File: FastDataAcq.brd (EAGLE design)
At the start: 114.3 x 63.5 mm, 215 parts, among them J1 MICRO-FIT_3.0_2POS_RA_SMD, J2 USB_MICROAB_SMT, U1 ADC08D500, U10 TMP421, U11 DAC101C081, U12 ADCMP553BRMZ, U13 XCFXXS04, U14 FT230XQ, U2 XC6SLX9-3TQG144C, U3 LTC2955-1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

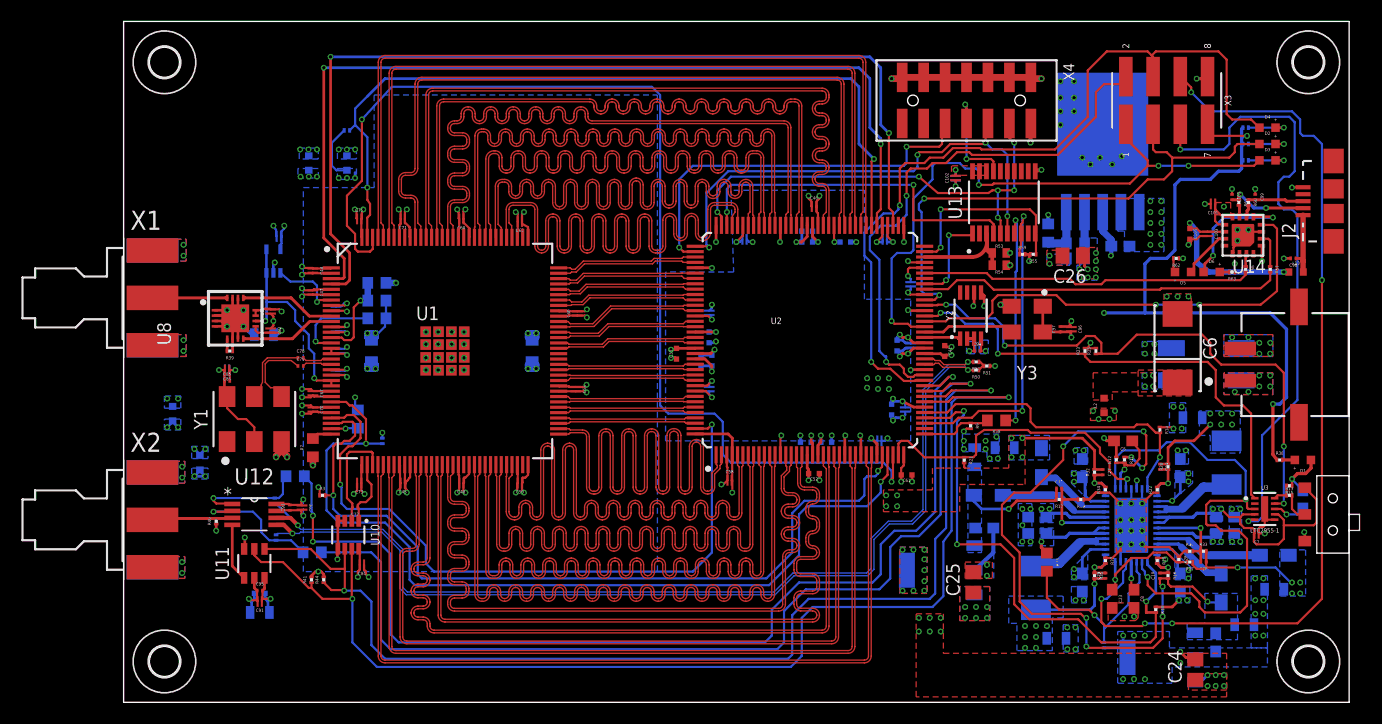
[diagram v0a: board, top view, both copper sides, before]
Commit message: FDA v0.9 Ready For Quote Submission
All that is left is shielding mounting holes.
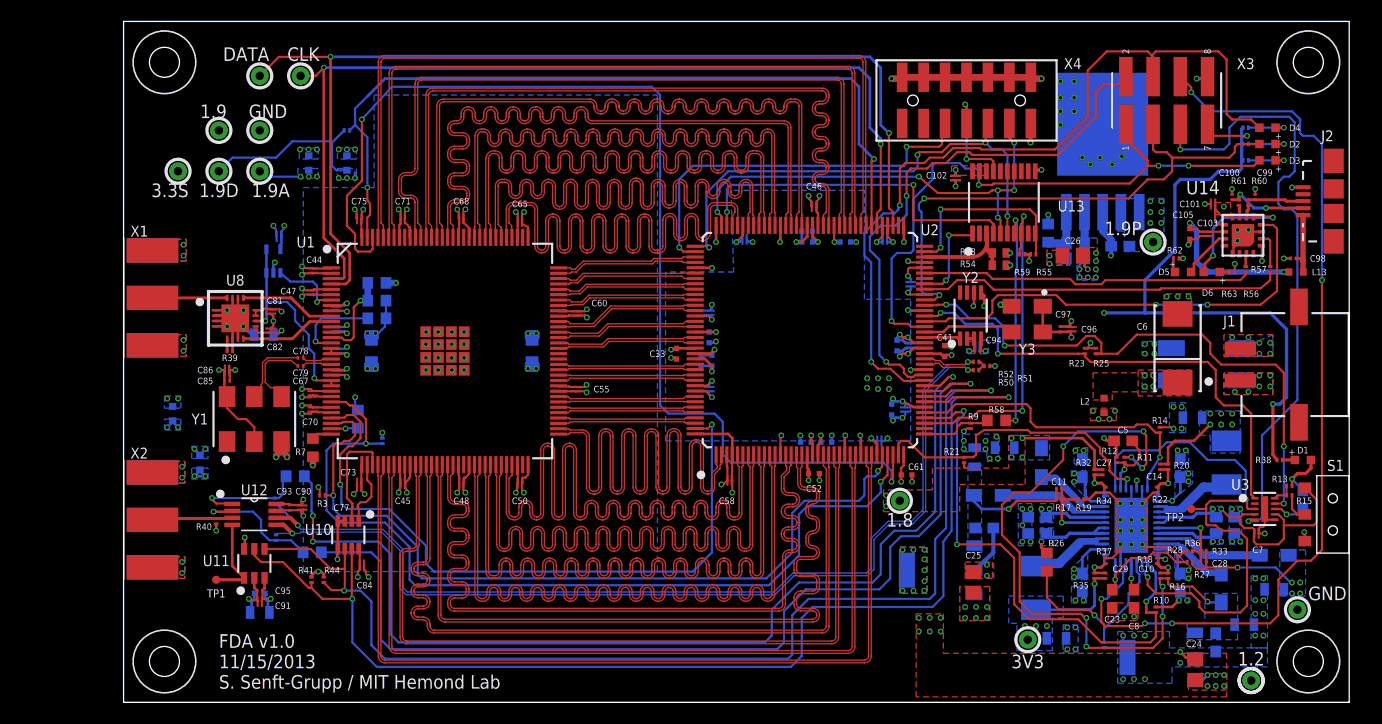
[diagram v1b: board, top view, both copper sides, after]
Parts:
- added TP1, TP2: TEST-POINT3, SparkFun-Passives:PAD.03X.03
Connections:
- net PWR_ENABLE: now also TP2.P$1
- net TRIG_REF: now also TP1.P$1
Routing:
- net 1V9D: track 31.3 -> 43.1 mm, vias 14 -> 15
- net ADC_OUTEDGE/DDR/SDATA: track 90.3 -> 97.7 mm, vias 2 -> 3
- net 1V9A: track 33.4 -> 37.4 mm, vias 18 -> 19
- net TRIG_REF: track 5.41 -> 8.08 mm
- net ADC_OUTV/SCLK: track 87.2 -> 89.7 mm, vias 2 -> 3
- net PWR_ENABLE: track 50.6 -> 52.0 mm
- net 3V3: track 125.7 -> 124.8 mm, vias 34 -> 31
- net S_TEMP: track 87.9 -> 87.1 mm
- net GND: vias 214 -> 216
- net 3V3S: vias 5 -> 6
- net 2V3_1V9PRE: vias 16 -> 13
- net 1V9: vias 14 -> 15
- net 1V8: vias 17 -> 16
- net 1V2: vias 16 -> 17
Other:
- board text added: "1.2"
- board text added: "1.8"
- board text added: "1.9"
- board text added: "1.9A"
- board text added: "1.9D"
- board text added: "1.9P"
- board text added: "11/15/2013"
- board text added: "3.3S"
- board text added: "3V3"
- board text added: "CLK"
- board text added: "DATA"
- board text added: "FDA v1.0"
- board text added: "GND"
- board text added: "S. Senft-Grupp / MIT Hemond Lab"
- board text added: "TP1"
- board text added: "TP2"

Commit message: Neatened back traces.
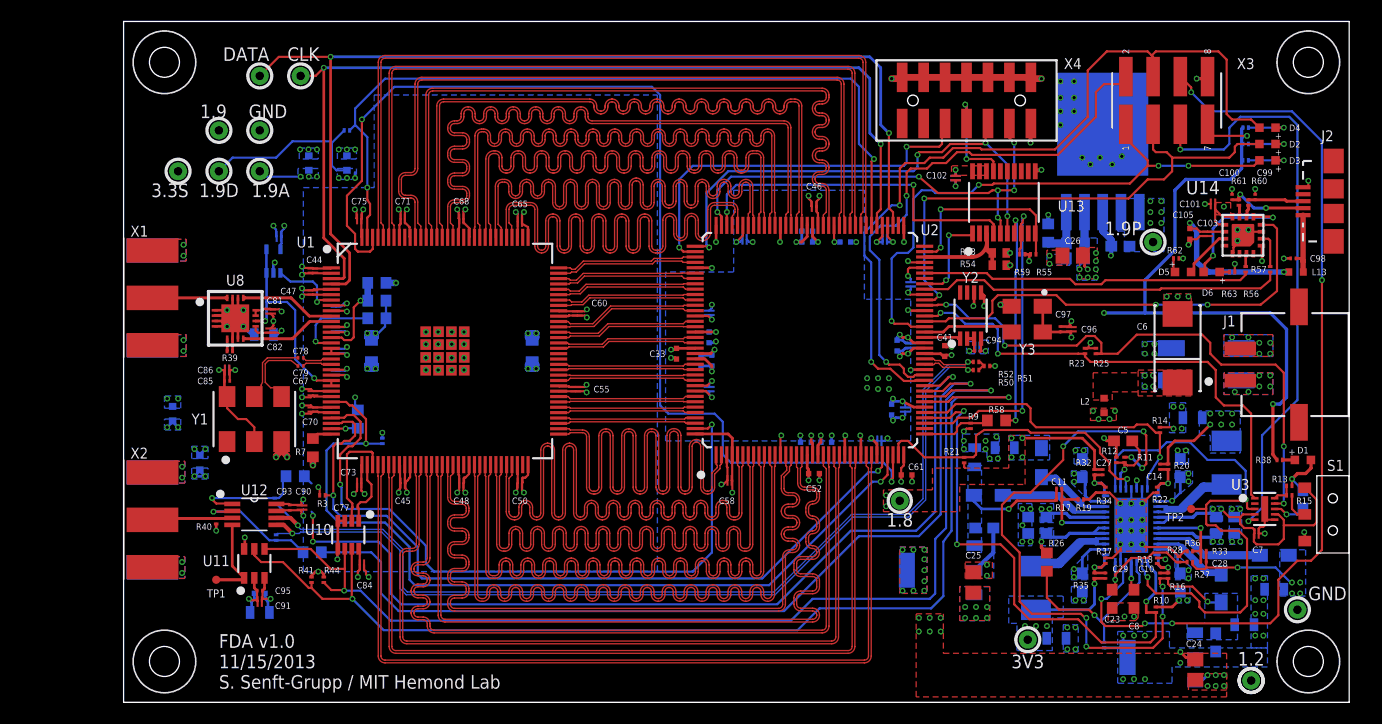
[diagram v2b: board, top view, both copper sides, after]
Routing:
- net TRIG_RESET_LOW: track 97.4 -> 86.6 mm
- net TRIG_RESET_HIGH: track 93.3 -> 84.3 mm
- net FPGA_SDA: track 108.7 -> 101.2 mm
- net FPGA_SCL: track 113.4 -> 106.1 mm
- net ADC_CAL: track 76.4 -> 73.2 mm
- net FPGA_GPIO3: track 58.0 -> 54.9 mm
- net ADC_PD: track 83.2 -> 80.4 mm
- net !PB: track 57.8 -> 55.3 mm
- net FPGA_TRIG_N: track 92.9 -> 90.7 mm
- net FPGA_TRIG_P: track 94.5 -> 92.2 mm
- net FPGA_GPIO4: track 51.4 -> 50.0 mm
- net N$20: track 12.5 -> 11.9 mm
- net S_TEMP: track 87.1 -> 86.5 mm
- net S_MODE: track 18.2 -> 17.6 mm
- net FPGA_TCK: track 47.4 -> 46.9 mm

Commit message: Minor Changes - Fixed Screw Holes
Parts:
- added PAD1, PAD2, PAD3, PAD4: (no value), wirepad:SMD1,27-2,54
- H1, H2, H3, H4: value MOUNT-HOLE2.8 -> MOUNT-HOLE2.0; device holes:2,8 -> holes:2.0
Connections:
- net GND: now also PAD1.1, PAD2.1, PAD3.1, PAD4.1
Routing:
- net GND: track 233.8 -> 243.5 mm, vias 216 -> 219
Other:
- board text added: "OFF"
- board text added: "ON"
- board text removed: "Manufacturer Notes: 1. All copper thickness is 1oz 2. LVDS lines are 5mil width with 5mil spacing and should have a 100 Ohms+/- 10% differential impedance."
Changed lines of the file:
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@@
 <layer number="1" name="Top" color="4" fill="1" visible="yes" active="yes"/>
 <layer number="2" name="GND" color="1" fill="3" visible="no" active="yes"/>
-<layer number="3" name="Power" color="3" fill="3" visible="no" active="yes"/>
+<layer number="3" name="Power" color="3" fill="3" visible="yes" active="yes"/>
 <layer number="14" name="Route14" color="1" fill="6" visible="no" active="no"/>
 <layer number="15" name="Route15" color="4" fill="6" visible="no" active="no"/>
@@
 <layer number="17" name="Pads" color="2" fill="1" visible="yes" active="yes"/>
 <layer number="18" name="Vias" color="2" fill="1" visible="yes" active="yes"/>
-<layer number="19" name="Unrouted" color="6" fill="1" visible="no" active="yes"/>
+<layer number="19" name="Unrouted" color="6" fill="1" visible="yes" active="yes"/>
 <layer number="20" name="Dimension" color="15" fill="1" visible="yes" active="yes"/>
 <layer number="21" name="tPlace" color="7" fill="1" visible="yes" active="yes"/>
-<layer number="22" name="bPlace" color="7" fill="1" visible="yes" active="yes"/>
+<layer number="22" name="bPlace" color="7" fill="1" visible="no" active="yes"/>
 <layer number="23" name="tOrigins" color="15" fill="1" visible="yes" active="yes"/>
-<layer number="24" name="bOrigins" color="15" fill="1" visible="yes" active="yes"/>
+<layer number="24" name="bOrigins" color="15" fill="1" visible="no" active="yes"/>
 <layer number="25" name="tNames" color="7" fill="1" visible="yes" active="yes"/>
-<layer number="26" name="bNames" color="7" fill="1" visible="yes" active="yes"/>
+<layer number="26" name="bNames" color="7" fill="1" visible="no" active="yes"/>
 <layer number="27" name="tValues" color="7" fill="1" visible="no" active="yes"/>
 <layer number="28" name="bValues" color="7" fill="1" visible="no" active="yes"/>
@@
 <layer number="49" name="Reference" color="7" fill="1" visible="no" active="yes"/>
 <layer number="50" name="dxf" color="7" fill="1" visible="no" active="no"/>
-<layer number="51" name="tDocu" color="14" fill="1" visible="no" active="yes"/>
+<layer number="51" name="tDocu" color="14" fill="1" visible="yes" active="yes"/>
 <layer number="52" name="bDocu" color="14" fill="1" visible="no" active="yes"/>
 <layer number="53" name="tGND_GNDA" color="7" fill="9" visible="no" active="no"/>
@@
 <wire x1="114.3" y1="63.5" x2="0" y2="63.5" width="0" layer="20"/>
 <wire x1="0" y1="63.5" x2="0" y2="0" width="0" layer="20"/>
-<text x="0.127" y="68.834" size="0.6096" layer="51">Manufacturer Notes:
-1. All copper thickness is 1oz
-2. LVDS lines are 5mil width with 5mil spacing and should have a  100 Ohms+/- 10% differential impedance.</text>
 <text x="13.462" y="55.118" size="1.27" layer="21" font="vector" align="center">GND</text>
 <text x="8.382" y="55.118" size="1.27" layer="21" font="vector" align="center">1.9</text>
@@
 <text x="84.328" y="3.81" size="1.27" layer="21" font="vector" align="center">3V3</text>
 <text x="72.39" y="17.018" size="1.27" layer="21" font="vector" align="center">1.8</text>
-<text x="112.268" y="10.16" size="1.27" layer="21" font="vector" align="center">GND</text>
+<text x="108.966" y="6.604" size="1.27" layer="21" font="vector" align="center">GND</text>
 <text x="93.218" y="44.196" size="1.27" layer="21" font="vector" align="center">1.9P</text>
 <circle x="5.08" y="49.53" radius="1.1176" width="0.3048" layer="21"/>
@@
 <text x="8.89" y="5.08" size="1.27" layer="21" font="vector">FDA v1.0</text>
 <text x="8.89" y="3.175" size="1.27" layer="21" font="vector">11/15/2013</text>
+<text x="113.284" y="21.59" size="1.27" layer="21" font="vector" rot="R90">ON</text>
+<text x="113.284" y="13.843" size="1.27" layer="21" font="vector" rot="R90" align="bottom-right">OFF</text>
+<circle x="3.81" y="59.69" radius="2" width="0.4064" layer="21"/>
 </plain>
 <attributes>
@@
 <attribute name="VALUE" x="77.7578" y="22.5924" size="0.6096" layer="27" font="vector" rot="R270" align="center"/>
 </element>
-<element name="H1" library="holes" package="2,8" value="MOUNT-HOLE2.8" x="110.49" y="3.81" smashed="yes"/>
-<element name="H2" library="holes" package="2,8" value="MOUNT-HOLE2.8" x="110.49" y="59.69" smashed="yes" rot="R90"/>
-<element name="H3" library="holes" package="2,8" value="MOUNT-HOLE2.8" x="3.81" y="3.81" smashed="yes" rot="R90"/>
-<element name="H4" library="holes" package="2,8" value="MOUNT-HOLE2.8" x="3.81" y="59.69" smashed="yes"/>
+<element name="H1" library="holes" package="2.0" value="MOUNT-HOLE2.0" x="110.49" y="3.81" smashed="yes"/>
+<element name="H2" library="holes" package="2.0" value="MOUNT-HOLE2.0" x="110.49" y="59.69" smashed="yes" rot="R90"/>
+<element name="H3" library="holes" package="2.0" value="MOUNT-HOLE2.0" x="3.81" y="3.81" smashed="yes" rot="R90"/>
+<element name="H4" library="holes" package="2.0" value="MOUNT-HOLE2.0" x="3.81" y="59.69" smashed="yes"/>
 <element name="D1" library="Schuyler" package="0603_LED" value="LED_0603_RED" x="109.982" y="22.606" smashed="yes" rot="R180">
 <attribute name="MANUFACTURER" value="" x="109.982" y="22.606" size="1.778" layer="27" rot="R180" display="off"/>
@@
 <attribute name="PARTNUMBER" value="401-2012-1-ND" x="112.776" y="17.526" size="1.778" layer="27" rot="R90" display="off"/>
 <attribute name="MANPARTNUMBER" value="AYZ0102AGRLC" x="112.776" y="17.526" size="1.778" layer="27" rot="R90" display="off"/>
-<attribute name="NAME" x="113.03" y="22.098" size="1.016" layer="25" font="vector" rot="R180" align="center"/>
+<attribute name="NAME" x="108.966" y="14.224" size="1.016" layer="25" font="vector" rot="R180" align="center"/>
 </element>
 <element name="R14" library="rcl" package="R0201" value="523K" x="96.647" y="25.4" smashed="yes" rot="R270">
@@
 <attribute name="PARTNUMBER" value="WM17450-ND" x="97.282" y="56.134" size="1.778" layer="27" display="off"/>
 <attribute name="MANPARTNUMBER" value="0015912080" x="97.282" y="56.134" size="1.778" layer="27" display="off"/>
-<attribute name="NAME" x="104.648" y="59.563" size="1.016" layer="21" font="vector" rot="R180" align="center"/>
+<attribute name="NAME" x="104.14" y="56.134" size="1.016" layer="21" font="vector" rot="R180" align="center"/>
 </element>
 <element name="TP1" library="SparkFun-Passives" package="PAD.03X.03" value="TEST-POINT3" x="8.636" y="11.43"/>
 <element name="TP2" library="SparkFun-Passives" package="PAD.03X.03" value="TEST-POINT3" x="99.568" y="18.034"/>
+<element name="PAD2" library="wirepad" package="SMD1,27-2,54" value="" x="112.014" y="8.636"/>
+<element name="PAD1" library="wirepad" package="SMD1,27-2,54" value="" x="3.81" y="8.636" rot="R90"/>
+<element name="PAD3" library="wirepad" package="SMD1,27-2,54" value="" x="3.81" y="54.864"/>
+<element name="PAD4" library="wirepad" package="SMD1,27-2,54" value="" x="105.664" y="60.706"/>
 </elements>
 <signals>
@@
 <wire x1="110.393" y1="48.036" x2="110.49" y2="48.133" width="0.2032" layer="1"/>
 <wire x1="110.49" y1="48.133" x2="110.49" y2="48.641" width="0.2032" layer="1"/>
+<contactref element="PAD4" pad="1"/>
+<contactref element="PAD3" pad="1"/>
+<contactref element="PAD2" pad="1"/>
+<contactref element="PAD1" pad="1"/>
+<via x="6.858" y="8.636" extent="1-16" drill="0.3048"/>
+<wire x1="6.858" y1="8.636" x2="3.81" y2="8.636" width="0.6096" layer="1"/>
+<via x="5.842" y="54.864" extent="1-16" drill="0.3048"/>
+<wire x1="3.81" y1="54.864" x2="5.842" y2="54.864" width="0.6096" layer="1"/>
+<wire x1="109.474" y1="8.636" x2="112.014" y2="8.636" width="0.6096" layer="1"/>
+<via x="105.664" y="58.674" extent="1-16" drill="0.3048"/>
+<wire x1="105.664" y1="58.674" x2="105.664" y2="60.706" width="0.6096" layer="1"/>
 </signal>
 <signal name="N$8">

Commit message: More minor fixes.
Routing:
- net FPGA_TDO: track 32.5 -> 31.6 mm
- net CLK500_N: track 6.99 -> 6.29 mm
- net CLK500_P: track 7.27 -> 6.63 mm

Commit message: Ready for quote submittal.
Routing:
- net GND: track 243.2 -> 241.7 mm

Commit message: Done with adjusting most of the LVDS track widths.
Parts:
- added R64, R65, R66, R67: 330, rcl:R0201
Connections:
- new net N$23: R65.1, X3.P$2
- new net N$25: R66.1, X3.P$3
- new net N$26: R67.1, X3.P$4
- new net N$9: R64.1, X3.P$1
- net FPGA_GPIO1: now also R67.2; no longer X3.P$4
- net FPGA_GPIO2: now also R65.2; no longer X3.P$2
- net FPGA_GPIO3: now also R64.2; no longer X3.P$1
- net FPGA_GPIO4: now also R66.2; no longer X3.P$3
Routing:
- net N$26: track 0.00 -> 12.7 mm
- net ADC_DCLKRST: track 8.22 -> 0.00 mm, vias 1 -> 0
- net FPGA_GPIO2: track 51.5 -> 43.3 mm
- net N$9: track 0.00 -> 7.79 mm
- net N$23: track 0.00 -> 7.74 mm
- net FPGA_GPIO4: track 50.0 -> 44.5 mm
- net N$25: track 0.00 -> 4.00 mm
- net FPGA_TDI: track 37.0 -> 40.8 mm
- net FPGA_GPIO3: track 54.9 -> 51.3 mm
- net DQD0_N: track 82.6 -> 81.2 mm
- net DQD0_P: track 83.1 -> 82.0 mm
- net FPGA_GPIO1: track 74.8 -> 73.7 mm
- net DQD5_P: track 73.2 -> 74.2 mm
- net DQD2_P: track 75.5 -> 76.5 mm
- net DQD2_N: track 74.8 -> 75.8 mm
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
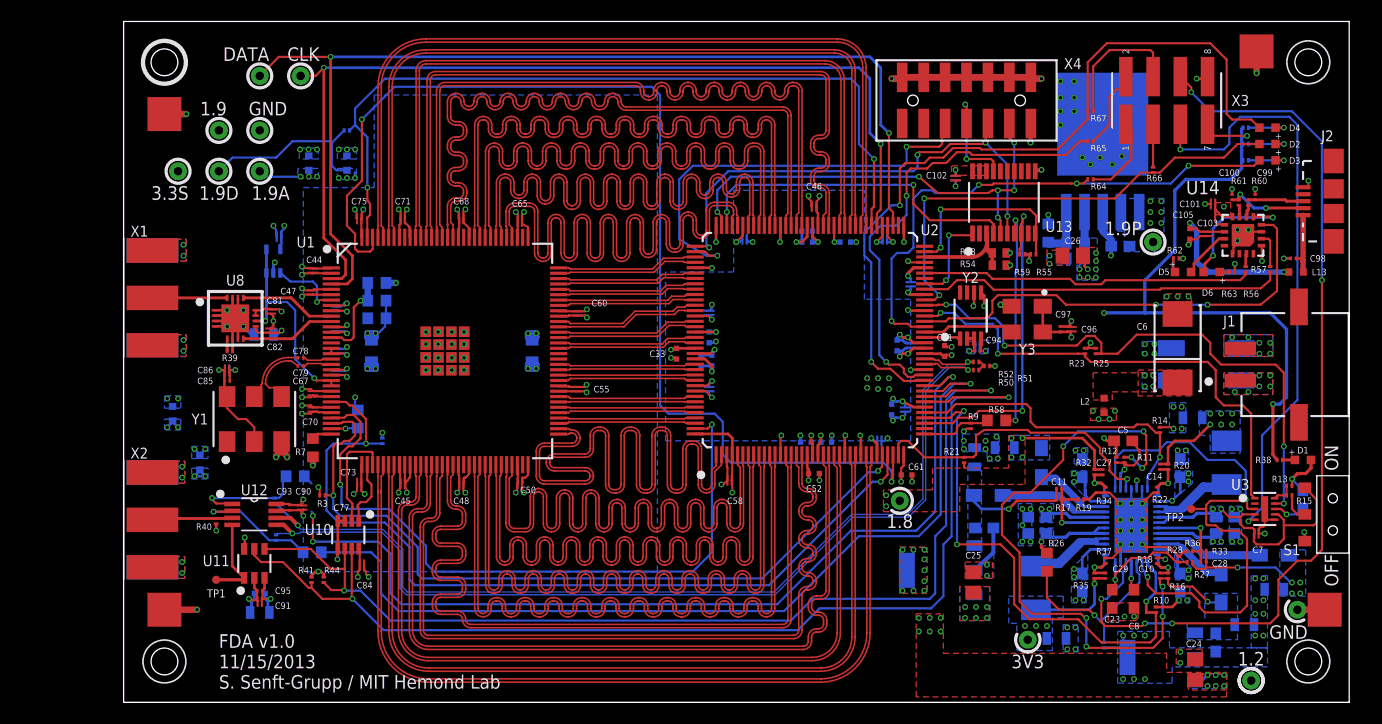
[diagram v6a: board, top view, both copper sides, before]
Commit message: Bottom LVDS traces optimized
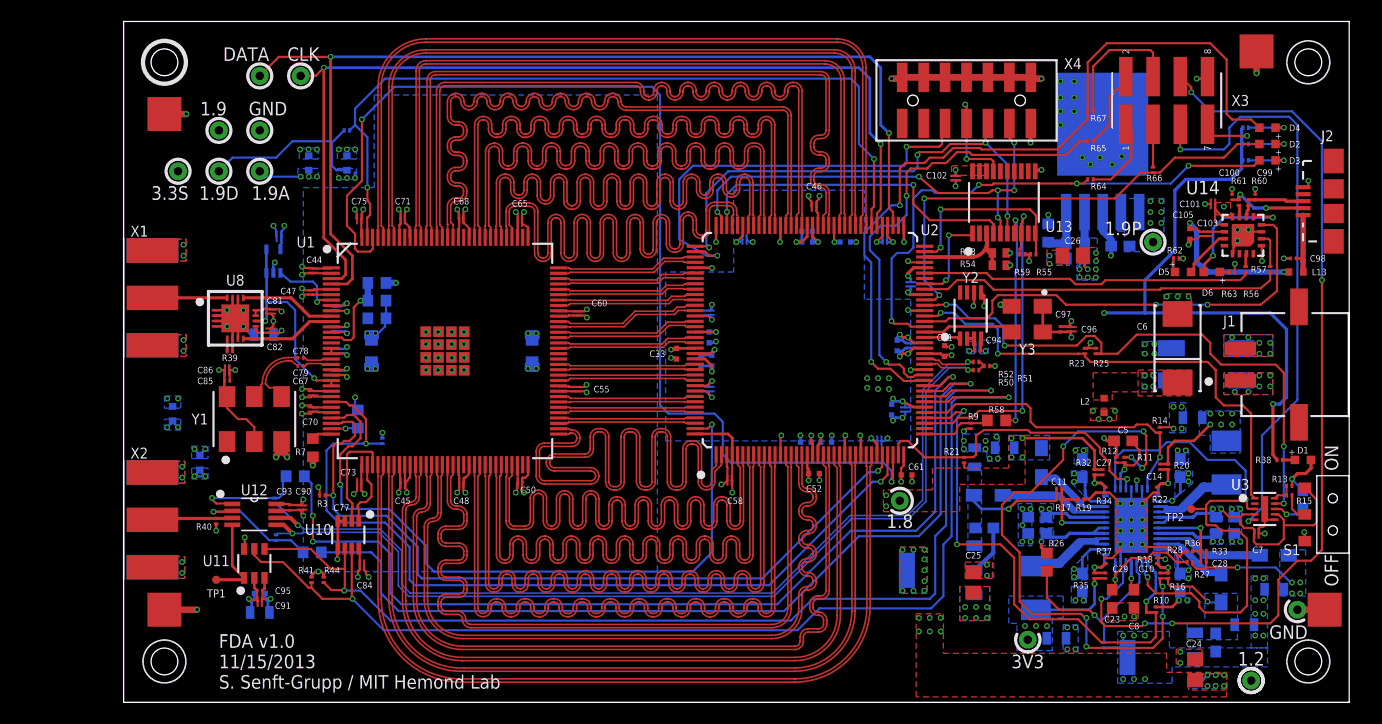
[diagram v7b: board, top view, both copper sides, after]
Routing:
- net DQD4_P: track 73.9 -> 70.4 mm
- net DQD4_N: track 73.1 -> 69.6 mm
- net DQD2_P: track 76.5 -> 73.2 mm
- net DQD2_N: track 75.8 -> 72.4 mm
- net DQD0_P: track 82.0 -> 78.8 mm
- net DQD0_N: track 81.2 -> 78.0 mm
- net DQD1_P: track 78.9 -> 75.7 mm
- net DQD1_N: track 78.2 -> 75.0 mm
- net DQD5_N: track 73.5 -> 70.6 mm
- net DQD5_P: track 74.2 -> 71.3 mm
- net DQD3_P: track 74.7 -> 72.0 mm
- net DQD3_N: track 73.9 -> 71.3 mm
- net TRIG_RESET_LOW: track 86.6 -> 89.1 mm
- net DQD7_P: track 71.8 -> 69.4 mm
- net DQD7_N: track 71.0 -> 68.6 mm
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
